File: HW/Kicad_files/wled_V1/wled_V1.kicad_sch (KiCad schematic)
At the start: 17 parts, among them J1 USB_C_Receptacle, J2 Jack-DC, J3 Conn_01x07_Pin, J5 Conn_01x04_Socket, J7 Conn_01x04_Socket, U1 ESP32-S3-WROOM-1, U3 TXS0102DCT

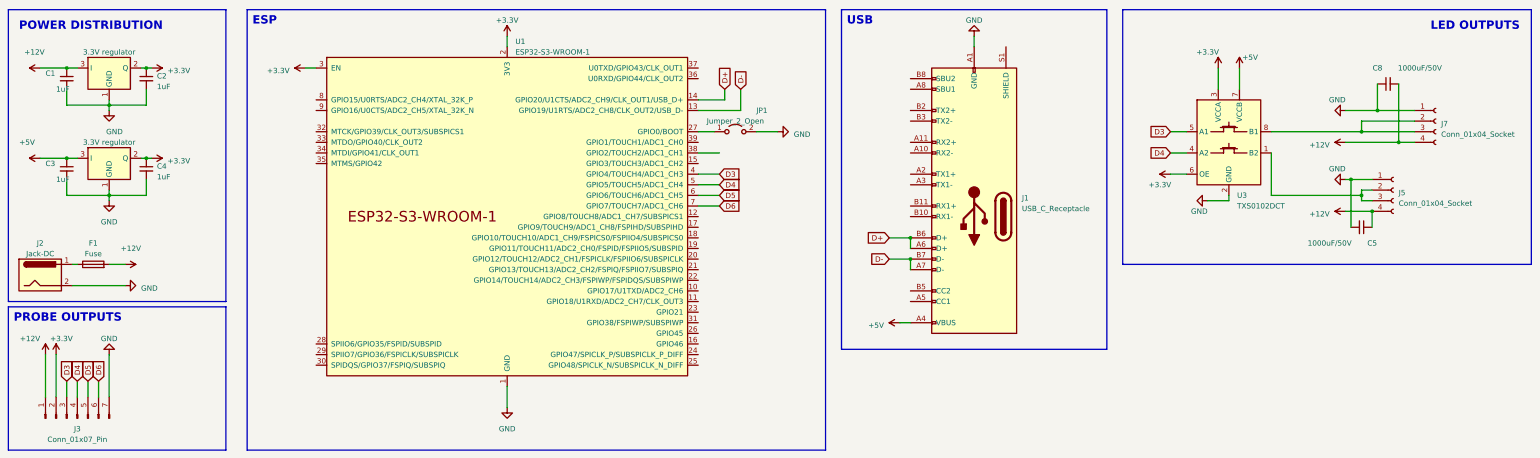
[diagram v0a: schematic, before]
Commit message: 5v removed
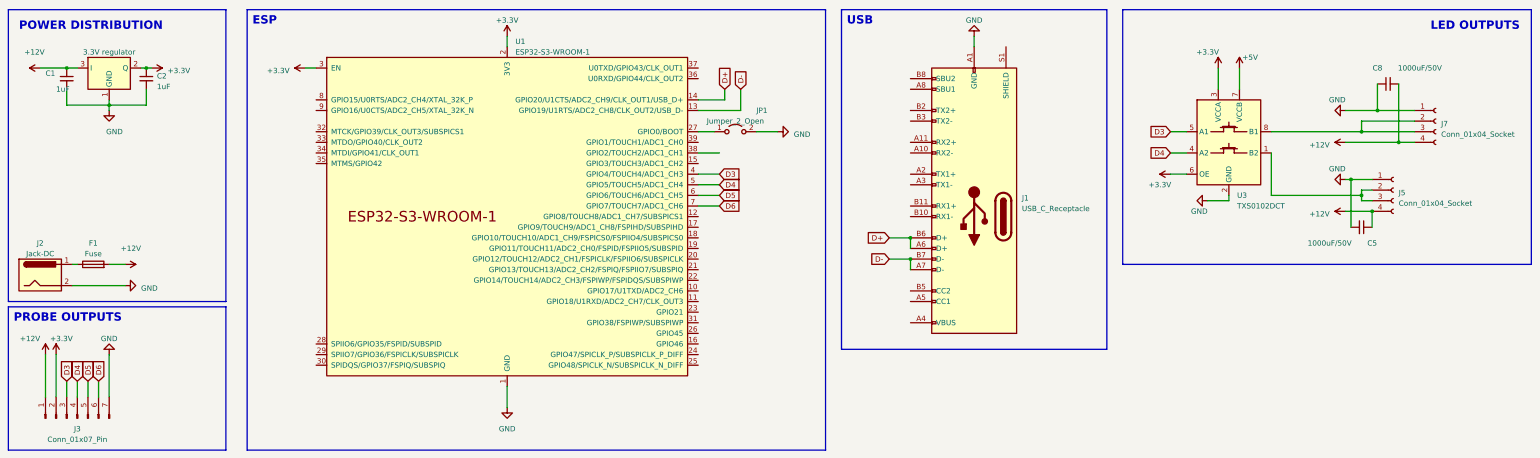
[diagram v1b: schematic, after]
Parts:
- removed C3, C4: 1uF, symbol Device:C_Small
- removed TLV75533PDBVR1: 3.3V regulator, Package_TO_SOT_SMD:TO-252-3_TabPin2, symbol Regulator_Linear:IFX27001TFV33
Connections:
- net +5V: no longer J1.A4 (VBUS), J1.A9 (VBUS), J1.B4 (VBUS), J1.B9 (VBUS)
- new net: J1.A4 (VBUS), J1.A9 (VBUS), J1.B4 (VBUS), J1.B9 (VBUS)

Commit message: Power supply update
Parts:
- added C3, C4: 1uF, symbol Device:C_Small
- added TLV75533PDBVR1: 12v to 5v, Package_TO_SOT_SMD:TO-252-3_TabPin2, symbol Regulator_Linear:IFX27001TFV33
- TLV75533PDBVR: value 3.3V regulator -> 5v to 3v3
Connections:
- net +12V: now also C3.1, TLV75533PDBVR1.3 (I); no longer C1.1, TLV75533PDBVR.3 (I)
- net +5V: now also C1.1, J1.A4 (VBUS), J1.A9 (VBUS), J1.B4 (VBUS), J1.B9 (VBUS), TLV75533PDBVR.3 (I), C4.1, TLV75533PDBVR1.2 (Q)
- net GND: now also C3.2, C4.2, TLV75533PDBVR1.1 (GND)

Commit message: Ajout filtrage
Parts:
- added C10, C11, C15, C6, C7, C9: 100nF, symbol Device:C_Small
- added C12, C13, C14: 1uF, symbol Device:C_Small
- C1, C2, C3, C4: value 1uF -> 100nF
- renumbered TLV75533PDBVR1 to TSR-1-2450, TLV75533PDBVR to TSR-1-2450
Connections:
- net GND is gone; now on net +3.3V: C1.2, C2.2, C3.2, C4.2, C5.2, C8.1, J1.A1 (GND), J1.A12 (GND), J1.B1 (GND), J1.B12 (GND), J2.2, J3.7 (Pin_7), J5.1 (Pin_1), J7.1 (Pin_1), JP1.2 (B), TSR-1-2450.1 (GND), TSR-1-2450.1 (GND), U1.1 (GND), U1.40 (GND), U1.41 (GND), U3.2 (GND)
- net +12V: now also C13.1
- net +3.3V: now also C10.1, C10.2, C11.2, C12.2, C13.2, C14.1, C14.2, C15.1, C15.2, C6.1, C6.2, C7.1, C7.2, C9.2
- net +5V: now also C11.1, C12.1, C9.1
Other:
- moved on the sheet: J3

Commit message: Debut sourcing
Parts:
- renumbered J1 to 10164359-00011LF, J5 to 39-30-3041, J7 to 39-30-3041, TSR-1-2450 to AZ1117CR-3.3TRG1, C7 to C0402C103K1RACAUTO, U1 to ESP32-S3-WROOM-1-N8, J2 to PJ-102AH1
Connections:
- net +3.3V: no longer 10164359-00011LF.A1 (GND), 10164359-00011LF.A12 (GND), 10164359-00011LF.B1 (GND), 10164359-00011LF.B12 (GND), 39-30-3041.1 (Pin_1), 39-30-3041.1 (Pin_1), AZ1117CR-3.3TRG1.1 (GND), C0402C103K1RACAUTO.2, C1.2, C10.2, C11.2, C12.2, C13.2, C14.2, C15.2, C2.2, C3.2, C4.2, C5.2, C6.1, C8.1, C9.2, ESP32-S3-WROOM-1-N8.1 (GND), ESP32-S3-WROOM-1-N8.40 (GND), ESP32-S3-WROOM-1-N8.41 (GND), J3.7 (Pin_7), JP1.2 (B), PJ-102AH1.2, TSR-1-2450.1 (GND), U3.2 (GND)
- new net GND: 10164359-00011LF.A1 (GND), 10164359-00011LF.A12 (GND), 10164359-00011LF.B1 (GND), 10164359-00011LF.B12 (GND), 39-30-3041.1 (Pin_1), 39-30-3041.1 (Pin_1), AZ1117CR-3.3TRG1.1 (GND), C0402C103K1RACAUTO.2, C1.2, C10.2, C11.2, C12.2, C13.2, C14.2, C15.2, C2.2, C3.2, C4.2, C5.2, C6.1, C8.1, C9.2, ESP32-S3-WROOM-1-N8.1 (GND), ESP32-S3-WROOM-1-N8.40 (GND), ESP32-S3-WROOM-1-N8.41 (GND), J3.7 (Pin_7), JP1.2 (B), PJ-102AH1.2, TSR-1-2450.1 (GND), U3.2 (GND)
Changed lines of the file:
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@@
   (junction (at 29.21 35.56) (diameter 0) (color 0 0 0 0)
   )
-  (junction (at 26.035 26.67) (diameter 0) (color 0 0 0 0)
-  )
   (junction (at 335.28 54.61) (diameter 0) (color 0 0 0 0)
   )
@@
   (junction (at 346.71 45.72) (diameter 0) (color 0 0 0 0)
   )
-  (junction (at 133.35 22.86) (diameter 0) (color 0 0 0 0)
-  )
   (junction (at 118.11 22.86) (diameter 0) (color 0 0 0 0)
   )
@@
   (junction (at 229.87 68.58) (diameter 0) (color 0 0 0 0)
   )
-  (junction (at 127 22.86) (diameter 0) (color 0 0 0 0)
-  )
   (junction (at 127 17.145) (diameter 0) (color 0 0 0 0)
   )
@@
   (junction (at 41.275 80.01) (diameter 0) (color 0 0 0 0)
   )
+  (junction (at 20.32 26.67) (diameter 0) (color 0 0 0 0)
+  )
   (junction (at 29.21 26.67) (diameter 0) (color 0 0 0 0)
   )
@@
     (stroke (width 0) (type default))
   )
+  (wire (pts (xy 20.32 26.67) (xy 29.21 26.67))
+    (stroke (width 0) (type default))
+  )
   (wire (pts (xy 229.87 68.58) (xy 229.87 71.12))
     (stroke (width 0) (type default))
@@
     (stroke (width 0) (type default))
   )
-  (wire (pts (xy 26.035 23.495) (xy 26.035 26.67))
+  (wire (pts (xy 20.32 25.4) (xy 20.32 26.67))
     (stroke (width 0) (type default))
   )
@@
     (stroke (width 0) (type default))
   )
-  (wire (pts (xy 20.32 26.67) (xy 26.035 26.67))
-    (stroke (width 0) (type default))
-  )
-  (wire (pts (xy 127 22.86) (xy 133.35 22.86))
-    (stroke (width 0) (type default))
-  )
   (wire (pts (xy 29.21 80.01) (xy 41.275 80.01))
     (stroke (width 0) (type default))
@@
   )
   (wire (pts (xy 294.005 53.34) (xy 295.91 53.34))
-    (stroke (width 0) (type default))
-  )
-  (wire (pts (xy 26.035 26.67) (xy 29.21 26.67))
     (stroke (width 0) (type default))
   )
@@
     (effects (font (size 2 2) (thickness 0.4) bold) (justify left bottom))
   )
-  (text "POWER DISTRIBUTION\n" (at 16.51 19.05 0)
+  (text "POWER DISTRIBUTION\n" (at 14.605 17.145 0)
     (effects (font (size 2 2) (thickness 0.4) bold) (justify left bottom))
   )
@@
   (symbol (lib_id "Connector:Jack-DC") (at 21.59 77.47 0) (unit 1)
     (in_bom yes) (on_board yes) (dnp no) (fields_autoplaced)
-    (property "Reference" "J2" (at 21.59 69.85 0)
+    (property "Reference" "PJ-102AH1" (at 21.59 69.85 0)
       (effects (font (size 1.27 1.27)))
     )
@@
       (project "wled_V1"
         (path "/de2f0c7b-62aa-45a1-944c-ab4e5150c860"
-          (reference "J2") (unit 1)
+          (reference "PJ-102AH1") (unit 1)
         )
       )
@@
     )
   )
-  (symbol (lib_id "power:+5V") (at 26.035 23.495 0) (unit 1)
-    (in_bom yes) (on_board yes) (dnp no)
-    (property "Reference" "#PWR018" (at 26.035 27.305 0)
-      (effects (font (size 1.27 1.27)) hide)
-    )
-    (property "Value" "+5V" (at 27.305 21.59 0)
-      (effects (font (size 1.27 1.27)) (justify left))
-    )
-    (property "Footprint" "" (at 26.035 23.495 0)
-      (effects (font (size 1.27 1.27)) hide)
-    )
-    (property "Datasheet" "" (at 26.035 23.495 0)
+  (symbol (lib_id "power:+5V") (at 20.32 25.4 0) (unit 1)
+    (in_bom yes) (on_board yes) (dnp no)
+    (property "Reference" "#PWR018" (at 20.32 29.21 0)
+      (effects (font (size 1.27 1.27)) hide)
+    )
+    (property "Value" "+5V" (at 21.59 23.495 0)
+      (effects (font (size 1.27 1.27)) (justify left))
+    )
+    (property "Footprint" "" (at 20.32 25.4 0)
+      (effects (font (size 1.27 1.27)) hide)
+    )
+    (property "Datasheet" "" (at 20.32 25.4 0)
       (effects (font (size 1.27 1.27)) hide)
     )
@@
       (effects (font (size 1.27 1.27)) (justify left) hide)
     )
-    (property "Value" "100nF" (at 50.8 30.48 0)
+    (property "Value" "100nF" (at 48.895 32.385 0)
       (effects (font (size 1.27 1.27)) (justify left))
     )
@@
   (symbol (lib_id "Connector:Conn_01x04_Socket") (at 345.44 57.15 0) (unit 1)
     (in_bom yes) (on_board yes) (dnp no) (fields_autoplaced)
-    (property "Reference" "J5" (at 346.71 57.785 0)
+    (property "Reference" "39-30-3041" (at 346.71 57.785 0)
       (effects (font (size 1.27 1.27)) (justify left))
     )
@@
       (project "wled_V1"
         (path "/de2f0c7b-62aa-45a1-944c-ab4e5150c860"
-          (reference "J5") (unit 1)
+          (reference "39-30-3041") (unit 1)
         )
       )
@@
   (symbol (lib_id "Espressif:ESP32-S3-WROOM-1") (at 133.35 63.5 0) (unit 1)
     (in_bom yes) (on_board yes) (dnp no)
-    (property "Reference" "U1" (at 135.3059 21.59 0)
+    (property "Reference" "ESP32-S3-WROOM-1-N8" (at 135.3059 21.59 0)
       (effects (font (size 1.27 1.27)) (justify left))
     )
@@
       (project "wled_V1"
         (path "/de2f0c7b-62aa-45a1-944c-ab4e5150c860"
-          (reference "U1") (unit 1)
+          (reference "ESP32-S3-WROOM-1-N8") (unit 1)
         )
       )
@@
   )
   (symbol (lib_id "power:+3.3V") (at 49.53 26.67 270) (unit 1)
-    (in_bom yes) (on_board yes) (dnp no) (fields_autoplaced)
+    (in_bom yes) (on_board yes) (dnp no)
     (property "Reference" "#PWR07" (at 45.72 26.67 0)
       (effects (font (size 1.27 1.27)) hide)
     )
-    (property "Value" "+3.3V" (at 53.34 27.305 90)
+    (property "Value" "+3.3V" (at 52.705 26.67 90)
       (effects (font (size 1.27 1.27)) (justify left))
     )
@@
   (symbol (lib_id "Connector:Conn_01x04_Socket") (at 355.6 40.64 0) (unit 1)
     (in_bom yes) (on_board yes) (dnp no) (fields_autoplaced)
-    (property "Reference" "J7" (at 356.87 41.275 0)
+    (property "Reference" "39-30-3041" (at 356.87 41.275 0)
       (effects (font (size 1.27 1.27)) (justify left))
     )
@@
       (project "wled_V1"
         (path "/de2f0c7b-62aa-45a1-944c-ab4e5150c860"
-          (reference "J7") (unit 1)
+          (reference "39-30-3041") (unit 1)
         )
       )
@@
   (symbol (lib_id "Device:C_Small") (at 127 20.32 0) (unit 1)
     (in_bom yes) (on_board yes) (dnp no)
-    (property "Reference" "C7" (at 128.27 18.415 0)
+    (property "Reference" "C0402C103K1RACAUTO" (at 128.27 18.415 0)
       (effects (font (size 1.27 1.27)) (justify left) hide)
     )
@@
       (project "wled_V1"
         (path "/de2f0c7b-62aa-45a1-944c-ab4e5150c860"
-          (reference "C7") (unit 1)
+          (reference "C0402C103K1RACAUTO") (unit 1)
         )
       )
@@
       (effects (font (size 1.27 1.27)) (justify left) hide)
     )
-    (property "Value" "1uF" (at 14.605 30.48 0)
+    (property "Value" "1uF" (at 14.605 33.02 0)
       (effects (font (size 1.27 1.27)) (justify left))
     )
@@
   (symbol (lib_id "Regulator_Linear:IFX27001TFV33") (at 39.37 26.67 0) (unit 1)
     (in_bom yes) (on_board yes) (dnp no)
-    (property "Reference" "TSR-1-2450" (at 39.37 20.32 0)
-      (effects (font (size 1.27 1.27)) hide)
+    (property "Reference" "AZ1117CR-3.3TRG1" (at 39.37 20.955 0)
+      (effects (font (size 1.27 1.27)))
     )
     (property "Value" "5v to 3v3" (at 39.37 22.86 0)
@@
       (project "wled_V1"
         (path "/de2f0c7b-62aa-45a1-944c-ab4e5150c860"
-          (reference "TSR-1-2450") (unit 1)
+          (reference "AZ1117CR-3.3TRG1") (unit 1)
         )
       )
@@
   (symbol (lib_id "Connector:USB_C_Receptacle") (at 245.11 63.5 180) (unit 1)
     (in_bom yes) (on_board yes) (dnp no) (fields_autoplaced)
-    (property "Reference" "J1" (at 256.54 59.055 0)
+    (property "Reference" "10164359-00011LF" (at 256.54 59.055 0)
       (effects (font (size 1.27 1.27)) (justify right))
     )
@@
       (project "wled_V1"
         (path "/de2f0c7b-62aa-45a1-944c-ab4e5150c860"
-          (reference "J1") (unit 1)
-        )
-      )
+          (reference "10164359-00011LF") (unit 1)
+        )
+      )

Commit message: refs updated + lib
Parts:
- removed J3: Conn_01x07_Pin, symbol Connector:Conn_01x07_Pin
- added TP1, TP2, TP3, TP4, TP5, TP6, TP7: TestPoint, TestPoint:TestPoint_THTPad_2.0x2.0mm_Drill1.0mm, symbol Connector:TestPoint
- 0440007.WRA1: renamed from F1; footprint (none) -> SamacSys_Parts:FUSC3216X85N
- 10164359-00011LF1: renamed from 10164359-00011LF; footprint (none) -> SamacSys_Parts:1016435900011LF
- 39-30-3041: footprint (none) -> SamacSys_Parts:39303041
- 39-30-3041-bis1: renamed from 39-30-3041; footprint (none) -> SamacSys_Parts:39303041
- C0402C103K1RACAUTO1: renamed from C0402C103K1RACAUTO; footprint (none) -> SamacSys_Parts:CAPC1005X55N
- C1, C10, C11, C12, C13, C14, C2, C3, C4, C6, C9: footprint (none) -> SamacSys_Parts:CAPC1005X55N
- C15, C5, C8: footprint (none) -> SamacSys_Parts:CAPAE1030X1030N
- JP1: footprint (none) -> Jumper:SolderJumper-2_P1.3mm_Bridged2Bar_Pad1.0x1.5mm
- PJ-057AH1: renamed from PJ-102AH1; footprint (none) -> SamacSys_Parts:PJ057AH
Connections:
- net +12V: now also TP1.1
- net +3.3V: now also TP2.1
- net D3: now also TP3.1
- net D4: now also TP4.1
- net D5: now also TP5.1
- net D6: now also TP6.1
- net GND: now also TP7.1

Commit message: routing update
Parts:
- ESP32-S3-WROOM-1-N8: footprint Espressif:ESP32-S3-WROOM-1 -> SamacSys_Parts:ESP32S3WROOM1N8R8
- TSR-1-2450: footprint Package_TO_SOT_SMD:TO-252-3_TabPin2 -> SamacSys_Parts:TSR12450
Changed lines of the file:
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@@
       (effects (font (size 1.27 1.27)) (justify left))
     )
-    (property "Footprint" "Espressif:ESP32-S3-WROOM-1" (at 135.89 111.76 0)
+    (property "Footprint" "SamacSys_Parts:ESP32S3WROOM1N8R8" (at 135.89 111.76 0)
       (effects (font (size 1.27 1.27)) hide)
     )
@@
       (effects (font (size 1.27 1.27)))
     )
-    (property "Footprint" "Package_TO_SOT_SMD:TO-252-3_TabPin2" (at 39.37 53.34 0)
-      (effects (font (size 1.27 1.27)) hide)
-    )
+    (property "Footprint" "SamacSys_Parts:TSR12450" (at 39.37 53.34 0)
+      (effects (font (size 1.27 1.27)) hide)
+    )
